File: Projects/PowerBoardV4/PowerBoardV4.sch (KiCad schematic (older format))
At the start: 0 parts

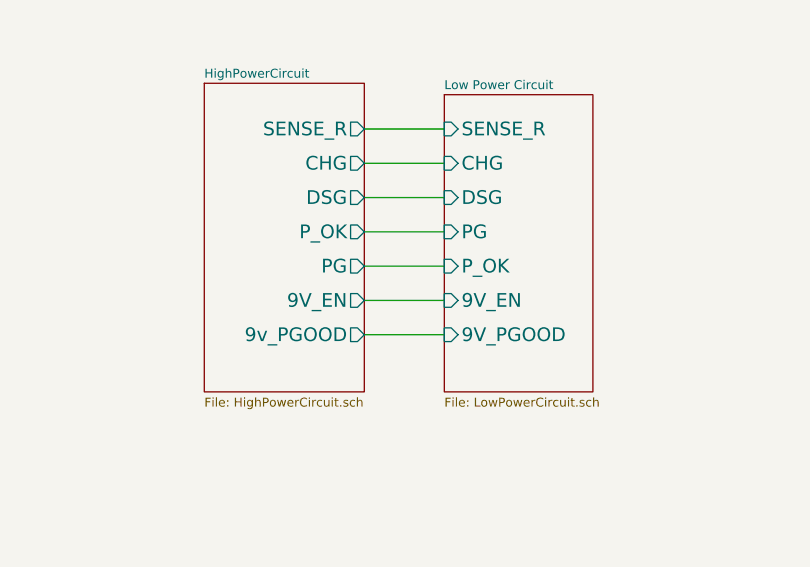
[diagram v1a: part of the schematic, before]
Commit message: modified the PowerBoard V4 schematic, left a comment by the usb connector
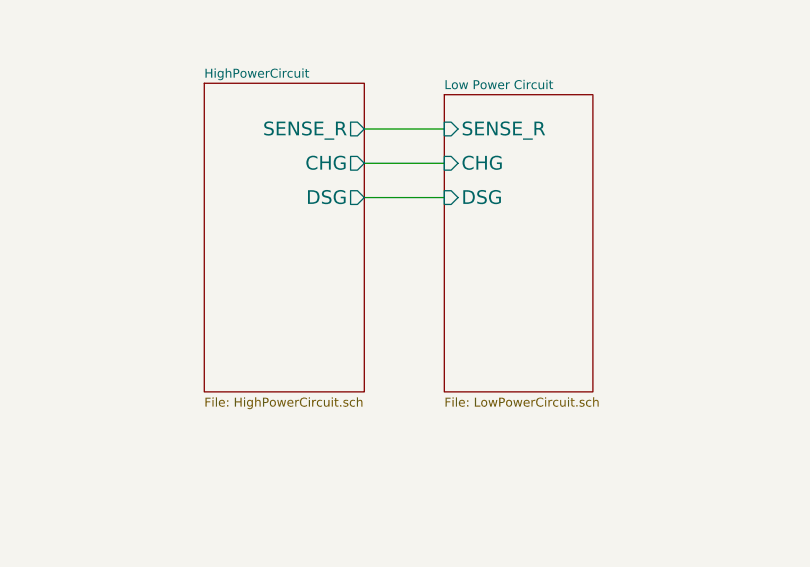
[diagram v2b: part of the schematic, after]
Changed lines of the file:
@@
 LIBS:switches
 LIBS:relays
+LIBS:motors
 LIBS:transistors
 LIBS:conn
@@
 Comment4 ""
 $EndDescr
+Wire Wire Line
+	5650 3100 6000 3100
+Wire Wire Line
+	5650 3250 6000 3250
+Wire Wire Line
+	5650 3400 6000 3400
+Text Notes 7350 7500 0    60   ~ 0
+Power Board Complete circuit
+Text Notes 2650 1100 0    60   ~ 0
+All GNDs are connected to the negative of the last cell. BATT- is not GND. \nThere is a separation between GND and BATT- using Power Transistors. \nThis can be seen on the layout example for the BQ76930 on Page 48\n
+Text Notes 3750 750  0    118  ~ 0
+IMPORTANT
 $Sheet
 S 4950 2900 700  1350
@@
 F3 "CHG" O R 5650 3250 60
 F4 "DSG" O R 5650 3400 60
-F5 "P_OK" O R 5650 3550 60
-F6 "PG" O R 5650 3700 60
-F7 "9V_EN" O R 5650 3850 60
-F8 "9v_PGOOD" O R 5650 4000 60
 $EndSheet
 $Sheet
@@
 F3 "CHG" I L 6000 3250 60
 F4 "DSG" I L 6000 3400 60
-F5 "PG" I L 6000 3550 60
-F6 "P_OK" I L 6000 3700 60
-F7 "9V_EN" I L 6000 3850 60
-F8 "9V_PGOOD" I L 6000 4000 60
 $EndSheet
-Wire Wire Line
-	5650 3100 6000 3100
-Wire Wire Line
-	5650 3250 6000 3250
-Wire Wire Line
-	5650 3400 6000 3400
-Wire Wire Line
-	5650 3550 6000 3550
-Wire Wire Line
-	5650 3700 6000 3700
-Wire Wire Line
-	5650 3850 6000 3850
-Wire Wire Line
-	5650 4000 6000 4000
-Text Notes 7350 7500 0    60   ~ 0
-Power Board Complete circuit
-Text Notes 2650 1100 0    60   ~ 0
-All GNDs are connected to the negative of the last cell. BATT- is not GND. \nThere is a separation between GND and BATT- using Power Transistors. \nThis can be seen on the layout example for the BQ76930 on Page 48\n
-Text Notes 3750 750  0    118  ~ 0
-IMPORTANT
 $EndSCHEMATC
